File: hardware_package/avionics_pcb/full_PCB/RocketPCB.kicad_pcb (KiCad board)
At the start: 4 copper layers, 0.8 x 1 mm, 72 parts, among them J1 DX07S024XJ1R1100, J2 Micro_SD_Card, J3 Conn_01x03_Female, M1 Motor_Servo_JR, M2 Motor_Servo_JR, Q1 DMG2301L, Q2 DMG2301L, SW1 SW_Push, SW2 SW_Push, U1 STM32F405RGTx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

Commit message: Updated with the correct version
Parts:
- J1: value DX07S024XJ1R1100 -> USB_C_Receptacle; footprint DX07S024XJ1R1100:JAE_DX07S024XJ1R1100 -> Connector_USB:USB_C_Receptacle_Palconn_UTC16-G
- moved J1 6.35 mm to (69.4, 75.6)
- moved U8 0.64 mm to (136.7, 83.7)
- moved U3 0.25 mm to (135.4, 57.4)
- moved U4 0.25 mm to (153.4, 62.5)
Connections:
- R3 pad 1: GND -> Net-(J1-PadB5)
- R3 pad 2: Net-(J1-PadB5) -> GND
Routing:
- net /D+: track 47.3 -> 59.1 mm
- net Net-(C8-Pad1): track 79.1 -> 68.2 mm, vias 0 -> 2
- net GND: track 201.3 -> 211.2 mm
- net /D-: track 50.1 -> 56.1 mm
- net ~RESET~: track 90.1 -> 95.3 mm, vias 0 -> 2
- net VBUS: track 17.1 -> 21.2 mm, vias 0 -> 2
- net +6V: track 43.0 -> 39.8 mm, vias 0 -> 1
- net +3V3: track 114.2 -> 111.3 mm
- net Net-(J1-PadA5): track 15.0 -> 17.9 mm
- net Net-(J1-PadB5): track 9.87 -> 12.7 mm
- net Net-(J1-PadS1): track 15.2 -> 17.0 mm
- net Net-(C4-Pad1): track 11.5 -> 12.4 mm
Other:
- board size 0.8 x 1 mm -> 88.3 x 29 mm
- board text added: "Avionics Package - Project Beans"
- board text added: "Flash Memory"
- board text added: "GPS"
- board text added: "MPU-6050"
- board text added: "Radio Header"
- board text added: "Servo 1"
- board text added: "Servo 2"
- board text removed: "Group 3 Avionics PCB"

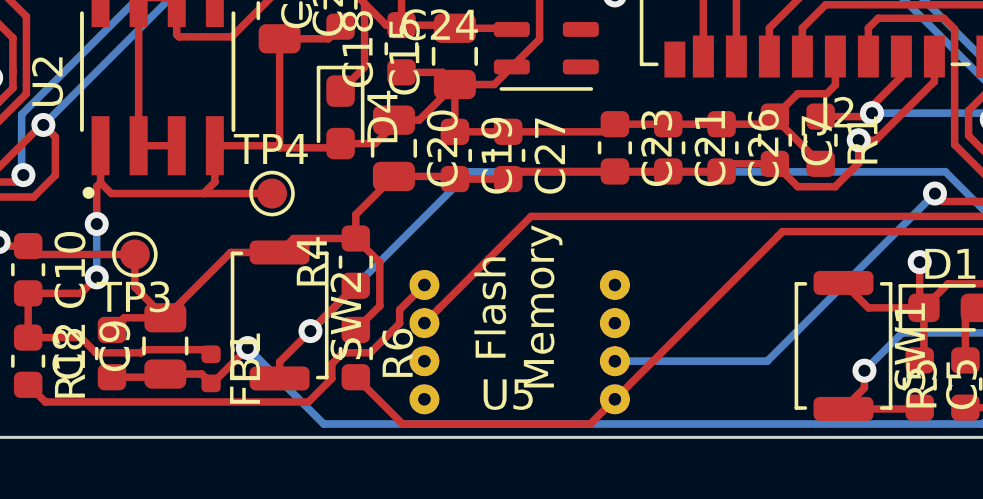
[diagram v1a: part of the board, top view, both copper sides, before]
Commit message: Labelled reset/boot buttons
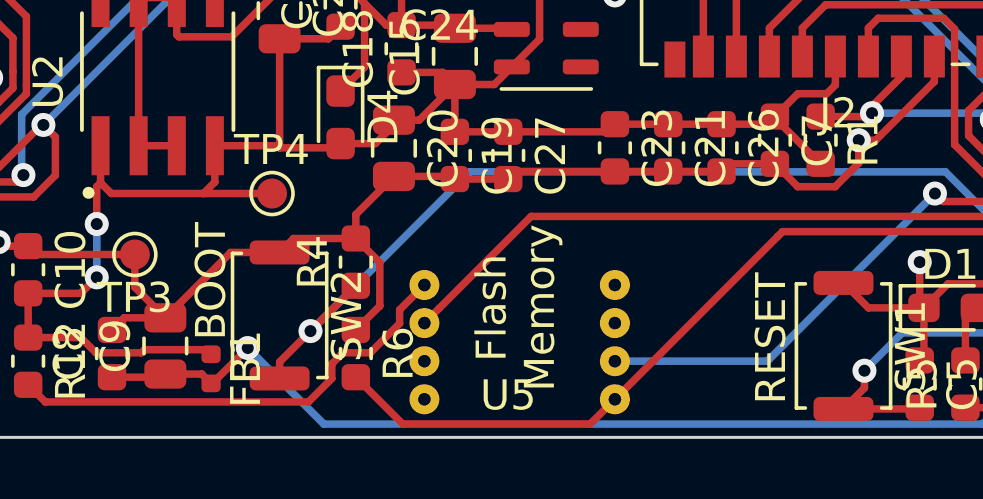
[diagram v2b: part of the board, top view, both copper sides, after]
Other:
- board text added: "BOOT"
- board text added: "RESET"
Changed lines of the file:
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@@
   (general
     (thickness 1.6)
-    (drawings 15)
+    (drawings 17)
     (tracks 622)
     (zones 0)
@@
   (layers
     (0 F.Cu signal)
-    (1 GND power hide)
-    (2 PWR power hide)
+    (1 GND power)
+    (2 PWR power)
     (31 B.Cu signal)
     (32 B.Adhes user)
@@
     )
   )
+  (gr_text BOOT (at 83.312 79.121 90) (layer F.SilkS)
+    (effects (font (size 1 1) (thickness 0.15)))
+  )
+  (gr_text "RESET\n" (at 101.981 81.026 90) (layer F.SilkS)
+    (effects (font (size 1 1) (thickness 0.15)))
+  )
   (gr_text "Avionics Package - Project Beans" (at 138.557 59.944) (layer B.SilkS)
